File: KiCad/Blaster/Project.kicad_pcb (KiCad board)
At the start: 2 copper layers, 129.7 x 40.6 mm, 60 parts, among them J2 Power & Output Test Points, J3 Inputs Test Points, Q1 BUK9832-55A, Q2 BUK9832-55A, Q3 BUK9832-55A, SW1 Power, SW2 Fire, SW3 Freq Select, SW4 Fire Select, U1 TLV1117-50, U2 PIC16F1788-IP, U3 Audio Board

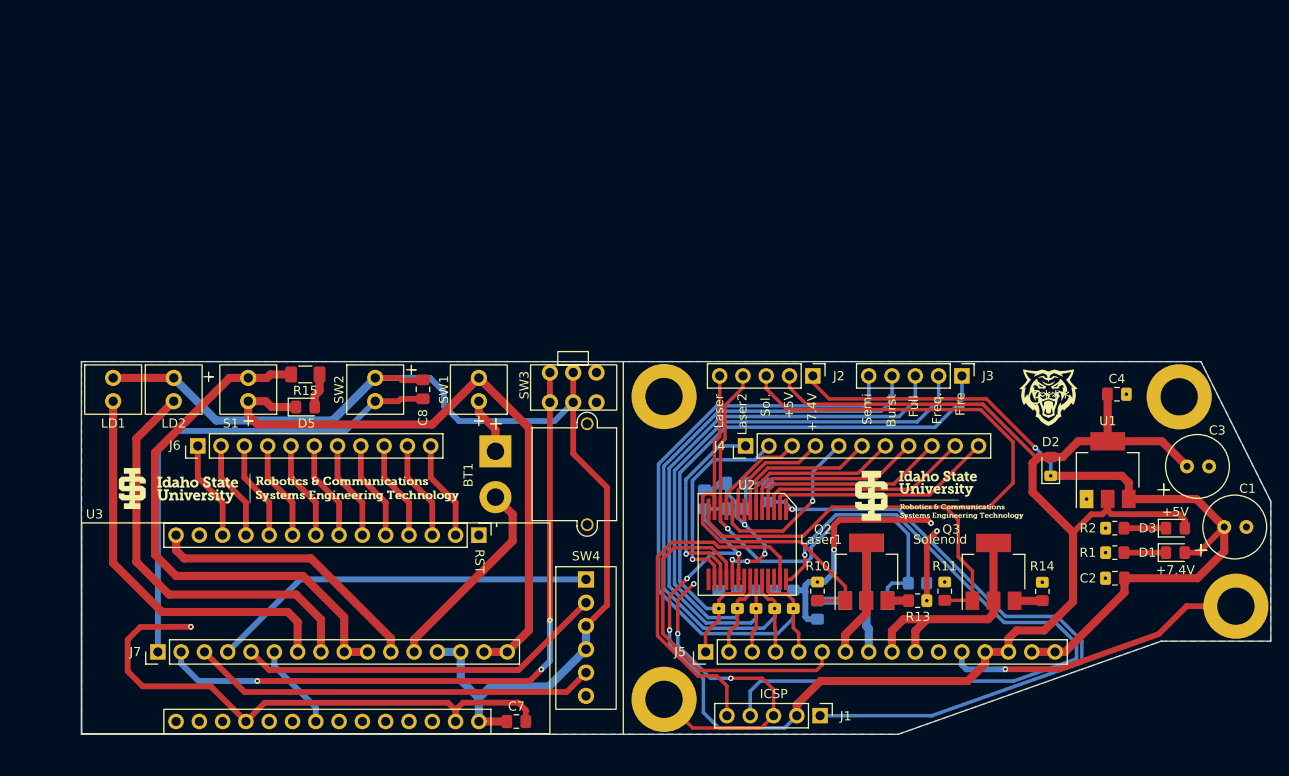
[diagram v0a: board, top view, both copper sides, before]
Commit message: Assign blaster footprints, Create Blaster PCB Outline
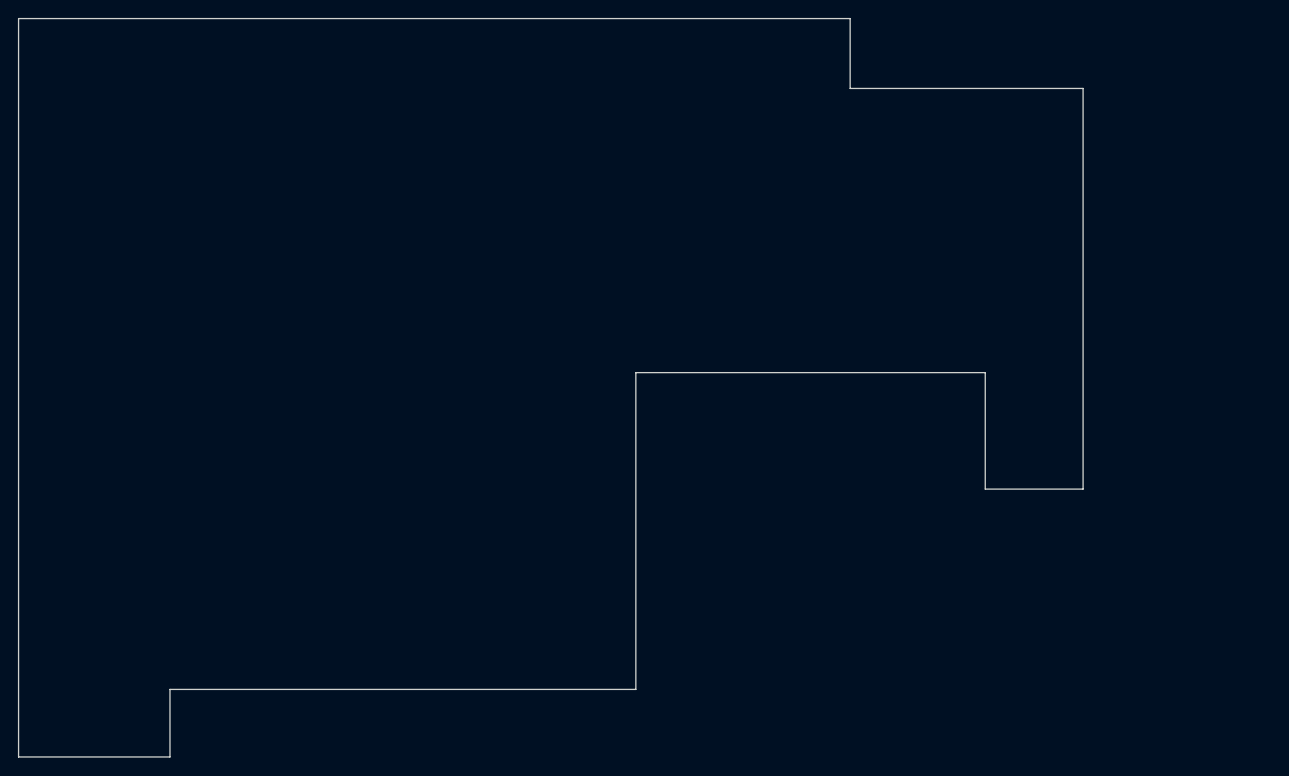
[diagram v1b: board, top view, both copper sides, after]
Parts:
- removed ? (x3): , 
- removed BT1: 7.4V, AlexWheelockFootprintLibrary:Project_Battery_Connector
- removed C1, C3: 220uF, AlexWheelockFootprintLibrary:Project_16V_220uF_Capacitor
- removed C2, C4: 0.1uF, Capacitor_SMD:C_0805_2012Metric_Pad1.18x1.45mm_HandSolder
- removed C5, C6, C7: 1uF, Capacitor_SMD:C_0805_2012Metric_Pad1.18x1.45mm_HandSolder
- removed C8: 50pF, Capacitor_SMD:C_0805_2012Metric_Pad1.18x1.45mm_HandSolder
- removed D1: +7.4V, LED_SMD:LED_0805_2012Metric_Pad1.15x1.40mm_HandSolder
- removed D2, D4, D5: 1N4148, Diode_SMD:D_0805_2012Metric_Pad1.15x1.40mm_HandSolder
- removed D3: +5V, LED_SMD:LED_0805_2012Metric_Pad1.15x1.40mm_HandSolder
- removed G*** (x7): LOGO, LOGO
- removed J1: ~, Connector_PinHeader_2.54mm:PinHeader_1x05_P2.54mm_Vertical
- removed J2: Power & Output Test Points, Connector_PinHeader_2.54mm:PinHeader_1x05_P2.54mm_Vertical
- removed J3: Inputs Test Points, Connector_PinHeader_2.54mm:PinHeader_1x05_P2.54mm_Vertical
- removed J4, J6: ~, Connector_PinHeader_2.54mm:PinHeader_1x11_P2.54mm_Vertical
- removed J5, J7: ~, Connector_PinHeader_2.54mm:PinHeader_1x16_P2.54mm_Vertical
- removed LD1, LD2: Laser Diode, AlexWheelockFootprintLibrary:Project_Locking_Output_Header
- removed Q1, Q2, Q3: BUK9832-55A, Package_TO_SOT_SMD:SOT-223-3_TabPin2
- removed R1: 8.2kΩ, Resistor_SMD:R_0805_2012Metric_Pad1.20x1.40mm_HandSolder
- removed R10, R11, R9: 100kΩ, Resistor_SMD:R_0805_2012Metric_Pad1.20x1.40mm_HandSolder
- removed R12, R13, R14: 0Ω, Resistor_SMD:R_0805_2012Metric_Pad1.20x1.40mm_HandSolder
- removed R15: 1kΩ, Resistor_SMD:R_1206_3216Metric_Pad1.30x1.75mm_HandSolder
- removed R2: 4.7kΩ, Resistor_SMD:R_0805_2012Metric_Pad1.20x1.40mm_HandSolder
- removed R3: 10kΩ, Resistor_SMD:R_0805_2012Metric_Pad1.20x1.40mm_HandSolder
- removed R4, R5, R6, R7, R8: 330Ω, Resistor_SMD:R_0805_2012Metric_Pad1.20x1.40mm_HandSolder
- removed REF**: 6-32 Mount, AlexWheelockFootprintLibrary:6-32 Mount
- removed S1: Solenoid, AlexWheelockFootprintLibrary:Project_Locking_Output_Header
- removed SW1: Power, AlexWheelockFootprintLibrary:Project_Locking_Output_Header
- removed SW2: Fire, AlexWheelockFootprintLibrary:Project_Locking_Output_Header
- removed SW3: Freq Select, AlexWheelockFootprintLibrary:Project_Blaster_Freq_Switch
- removed SW4: Fire Select, AlexWheelockFootprintLibrary:Project_Locking_Header_1x06
- removed U1: TLV1117-50, Package_TO_SOT_SMD:SOT-223-3_TabPin2
- removed U2: PIC16F1788-IP, AlexWheelockFootprintLibrary:SSOP-28
- removed U3: Audio Board, AlexWheelockFootprintLibrary:Project_Audio_Board
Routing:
- net GND: track 239.0 -> 0.00 mm, vias 12 -> 0
- net +5V: track 176.0 -> 0.00 mm, vias 3 -> 0
- net +5V_Top: track 123.6 -> 0.00 mm
- net +7.4V: track 88.6 -> 0.00 mm, vias 1 -> 0
- net Net-(Q3-G): track 87.3 -> 0.00 mm
- net RB7: track 82.4 -> 0.00 mm, vias 1 -> 0
- net Frequency Select_Top: track 74.7 -> 0.00 mm, vias 3 -> 0
- net Net-(D4-K): track 73.1 -> 0.00 mm, vias 1 -> 0
- net Semi-Auto: track 71.0 -> 0.00 mm
- net +7.4V_Top: track 70.3 -> 0.00 mm
- net Burst: track 67.9 -> 0.00 mm
- net Full-Auto: track 65.9 -> 0.00 mm
- net Frequency Select: track 65.4 -> 0.00 mm
- net Fire: track 64.8 -> 0.00 mm
- net Solenoid_Top: track 59.3 -> 0.00 mm
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- removed copper zone on B.Cu, net GND
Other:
- board size 129.7 x 40.6 mm -> 116.1 x 80.5 mm
- board text added: "TOP HATCH"
- board text removed: "+5V"
- board text removed: "+7.4V"
- board text removed: "Burst"
- board text removed: "Fire"
- board text removed: "Freq."
- board text removed: "Full"
- board text removed: "GitHub"
- board text removed: "ICSP"
- board text removed: "Laser"
- board text removed: "Laser Arcade Blaster (Bottom) Rev. A Alex Wheelock Spring 2025"
- board text removed: "Laser Arcade Blaster (Top) Rev. A Alex Wheelock Spring 2025"
- board text removed: "Laser1"
- board text removed: "Laser2"
- board text removed: "RST"
- board text removed: "Semi"
- board text removed: "Sol."
- board text removed: "Solenoid"

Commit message: Assign blaster PCB Footprints
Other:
- board text added: "Button Line"
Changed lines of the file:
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@@
+	)
+	(gr_line
+		(start 50.292 96.012)
+		(end 136.906 96.012)
+		(stroke
+			(width 0.1)
+			(type default)
+		)
+		(layer "B.Fab")
 	)
 	(gr_line
@@
 		(layer "F.Fab")
 	)
+	(gr_text "Button Line"
+		(at 58.928 96.012 0)
+		(layer "B.Fab")
+		(effects
+			(font
+				(size 1 1)
+				(thickness 0.15)
+			)
+			(justify left bottom mirror)
+		)
+	)
 	(gr_text "TOP HATCH"

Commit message: Place major components on PCB
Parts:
- added BT1: 18650, Battery:BatteryHolder_Keystone_1042_1x18650, F.Cu at (131.8, 61.7)
- added C1: 4.7µF, Capacitor_SMD:C_0805_2012Metric_Pad1.18x1.45mm_HandSolder, F.Cu at (-32.5, 95.3)
- added C10: 1uF, Capacitor_SMD:C_0805_2012Metric_Pad1.18x1.45mm_HandSolder, F.Cu at (-29.1, 167.0)
- added C11: 1uF, Capacitor_SMD:C_0805_2012Metric_Pad1.18x1.45mm_HandSolder, F.Cu at (-29.1, 170.0)
- added C12: 10nF, Capacitor_SMD:C_0805_2012Metric_Pad1.18x1.45mm_HandSolder, F.Cu at (-20.5, 123.6)
- added C13: 4.7µF, Capacitor_SMD:C_0805_2012Metric_Pad1.18x1.45mm_HandSolder, F.Cu at (-20.5, 126.6)
- added C14: 0.1µF, Capacitor_SMD:C_0805_2012Metric_Pad1.18x1.45mm_HandSolder, F.Cu at (-20.5, 129.6)
- added C15: 0.1µF, Capacitor_SMD:C_0805_2012Metric_Pad1.18x1.45mm_HandSolder, F.Cu at (-20.5, 132.6)
- added C16: 47pF, Capacitor_SMD:C_0805_2012Metric_Pad1.18x1.45mm_HandSolder, F.Cu at (-20.5, 135.6)
- added C17: 47pF, Capacitor_SMD:C_0805_2012Metric_Pad1.18x1.45mm_HandSolder, F.Cu at (-20.5, 138.6)
- added C2: 4.7µF, Capacitor_SMD:C_0805_2012Metric_Pad1.18x1.45mm_HandSolder, F.Cu at (-32.5, 98.3)
- added C3: 0.1µF, Capacitor_SMD:C_0805_2012Metric_Pad1.18x1.45mm_HandSolder, F.Cu at (-32.5, 101.3)
- added C4: 4.7µF, Capacitor_SMD:C_0805_2012Metric_Pad1.18x1.45mm_HandSolder, F.Cu at (-32.5, 104.3)
- added C5: 4.7µF, Capacitor_SMD:C_0805_2012Metric_Pad1.18x1.45mm_HandSolder, F.Cu at (-32.5, 107.3)
- added C6: 0.1µF, Capacitor_SMD:C_0805_2012Metric_Pad1.18x1.45mm_HandSolder, F.Cu at (-32.5, 110.3)
- added C7: 22µF, Capacitor_SMD:C_0805_2012Metric_Pad1.18x1.45mm_HandSolder, F.Cu at (-32.5, 113.3)
- added C8: 0.1µF, Capacitor_SMD:C_0805_2012Metric_Pad1.18x1.45mm_HandSolder, F.Cu at (-32.5, 116.3)
- added C9: 470pF, Capacitor_SMD:C_0805_2012Metric_Pad1.18x1.45mm_HandSolder, F.Cu at (113.8, 79.1)
- added D1: Charge, LED_SMD:LED_0805_2012Metric_Pad1.15x1.40mm_HandSolder, F.Cu at (10.3, 113.9)
- added D2: 1N4148, Diode_SMD:D_0805_2012Metric_Pad1.15x1.40mm_HandSolder, F.Cu at (-29.1, 173.0)
- added D3: IN-P32TRRRGB, 0_AKeller_Footprints:IN-P32TRRRGB, B.Cu at (117.9, 89.7)
- added D4: IN-P32TRRRGB, 0_AKeller_Footprints:IN-P32TRRRGB, B.Cu at (83.9, 85.8)
- added D5: TX, LED_SMD:LED_0805_2012Metric_Pad1.15x1.40mm_HandSolder, F.Cu at (-20.5, 141.6)
- added D6: RX, LED_SMD:LED_0805_2012Metric_Pad1.15x1.40mm_HandSolder, F.Cu at (-20.5, 144.7)
- added J1: +12V, 0_AKeller_Footprints:AMASS_XT60PW-M_1x02_P7.20mm_Horizontal, F.Cu at (77.1, 110.5)
- added J2: Speaker, 0_AKeller_Footprints:1x2_100mil_Header_Locking, F.Cu at (68.5, 83.7)
- added J3: ICSP, 0_AKeller_Footprints:1x6_100mil_Header, F.Cu at (-65.9, 172.4)
- added J4: Solenoid, 0_AKeller_Footprints:1x2_100mil_Header_Locking, F.Cu at (178.2, 51.6)
- added J5: Laser, 0_AKeller_Footprints:1x2_100mil_Header_Locking, F.Cu at (68.5, 46.4)
- added J6: Laser, 0_AKeller_Footprints:1x2_100mil_Header_Locking, F.Cu at (68.5, 56.9)
- added J7: USB_B_Micro, 0_AKeller_Footprints:USB_Micro-B_Amphenol, F.Cu at (97.4, 41.2)
- added L1: 6.8µH, 0_AKeller_Footprints:LA Blaster Power Inductor, F.Cu at (-13.2, 108.5)
- added L2: 2.2µH, Inductor_SMD:L_0805_2012Metric_Pad1.15x1.40mm_HandSolder, F.Cu at (-12.1, 135.2)
- added Q1: DMG3402L, Package_TO_SOT_SMD:SOT-23, F.Cu at (68.5, 88.7)
- added Q2: DMG3402L, Package_TO_SOT_SMD:SOT-23, F.Cu at (72.2, 88.7)
- added Q3: DMG3402L, Package_TO_SOT_SMD:SOT-23, F.Cu at (178.2, 56.7)
- added Q4: DMG3402L, Package_TO_SOT_SMD:SOT-23, F.Cu at (-38.4, 137.6)
- added R1: 2.2kΩ, Resistor_SMD:R_0805_2012Metric_Pad1.20x1.40mm_HandSolder, F.Cu at (-10.2, 95.2)
- added R10: 10kΩ, Resistor_SMD:R_0805_2012Metric_Pad1.20x1.40mm_HandSolder, F.Cu at (-36.8, 149.2)
- added R11: 10kΩ, Resistor_SMD:R_0805_2012Metric_Pad1.20x1.40mm_HandSolder, F.Cu at (177.2, 60.8)
- added R12: 330Ω, Resistor_SMD:R_0805_2012Metric_Pad1.20x1.40mm_HandSolder, F.Cu at (178.1, 73.5)
- added R13: 330Ω, Resistor_SMD:R_0805_2012Metric_Pad1.20x1.40mm_HandSolder, F.Cu at (-36.8, 158.0)
- added R14: 330Ω, Resistor_SMD:R_0805_2012Metric_Pad1.20x1.40mm_HandSolder, F.Cu at (-36.8, 161.0)
- added R15: 330Ω, Resistor_SMD:R_0805_2012Metric_Pad1.20x1.40mm_HandSolder, F.Cu at (-32.0, 149.2)
- added R16: 20Ω, Resistor_SMD:R_0805_2012Metric_Pad1.20x1.40mm_HandSolder, F.Cu at (124.1, 89.0)
- added R17: 20Ω, Resistor_SMD:R_0805_2012Metric_Pad1.20x1.40mm_HandSolder, F.Cu at (114.2, 87.0)
- added R18: 0Ω, Resistor_SMD:R_0805_2012Metric_Pad1.20x1.40mm_HandSolder, F.Cu at (69.5, 41.1)
- added R19: 0Ω, Resistor_SMD:R_0805_2012Metric_Pad1.20x1.40mm_HandSolder, F.Cu at (69.5, 51.8)
- added R2: 2.2kΩ, Resistor_SMD:R_0805_2012Metric_Pad1.20x1.40mm_HandSolder, F.Cu at (-10.2, 98.2)
- added R20: 260Ω, Resistor_SMD:R_0805_2012Metric_Pad1.20x1.40mm_HandSolder, F.Cu at (111.9, 90.5)
- added R21: 20Ω, Resistor_SMD:R_0805_2012Metric_Pad1.20x1.40mm_HandSolder, F.Cu at (77.7, 86.5)
- added R22: 20Ω, Resistor_SMD:R_0805_2012Metric_Pad1.20x1.40mm_HandSolder, F.Cu at (80.2, 83.0)
- added R23: 10kΩ, Resistor_SMD:R_0805_2012Metric_Pad1.20x1.40mm_HandSolder, F.Cu at (-27.3, 158.0)
- added R24: 260Ω, Resistor_SMD:R_0805_2012Metric_Pad1.20x1.40mm_HandSolder, F.Cu at (87.7, 82.4)
- added R25: 3.3kΩ, Resistor_SMD:R_0805_2012Metric_Pad1.20x1.40mm_HandSolder, F.Cu at (-12.1, 138.1)
- added R26: 3.3kΩ, Resistor_SMD:R_0805_2012Metric_Pad1.20x1.40mm_HandSolder, F.Cu at (-12.1, 141.1)
- added R27: 10kΩ, Resistor_SMD:R_0805_2012Metric_Pad1.20x1.40mm_HandSolder, F.Cu at (-12.1, 144.0)
- added R3: 47kΩ, Resistor_SMD:R_0805_2012Metric_Pad1.20x1.40mm_HandSolder, F.Cu at (-10.2, 101.2)
- added R4: 15kΩ, Resistor_SMD:R_0805_2012Metric_Pad1.20x1.40mm_HandSolder, F.Cu at (-10.2, 104.1)
- added R5: 10kΩ, Resistor_SMD:R_0805_2012Metric_Pad1.20x1.40mm_HandSolder, F.Cu at (113.8, 75.6)
- added R6: 1kΩ, Resistor_SMD:R_0805_2012Metric_Pad1.20x1.40mm_HandSolder, F.Cu at (68.5, 93.8)
- added R7: 20kΩ, Resistor_SMD:R_0805_2012Metric_Pad1.20x1.40mm_HandSolder, F.Cu at (122.2, 86.1)
- added R8: 10kΩ, Resistor_SMD:R_0805_2012Metric_Pad1.20x1.40mm_HandSolder, F.Cu at (74.1, 84.3)
- added R9: 20kΩ, Resistor_SMD:R_0805_2012Metric_Pad1.20x1.40mm_HandSolder, F.Cu at (125.5, 86.1)
- added SW1: Charge, 0_AKeller_Footprints:T80-T, F.Cu at (143.5, 44.2)
- added SW2: Power, 0_AKeller_Footprints:LA Blaster Power Switch, B.Cu at (83.9, 96.0)
- added SW3: Trigger, Button_Switch_THT:SW_Tactile_SPST_Angled_PTS645Vx31-2LFS, F.Cu at (177.0, 82.2)
- added SW4: Single, Button_Switch_THT:SW_PUSH_6mm_H5mm, B.Cu at (124.4, 98.3)
- added SW5: Burst, Button_Switch_THT:SW_PUSH_6mm_H5mm, B.Cu at (105.1, 98.3)
- added SW6: Auto, Button_Switch_THT:SW_PUSH_6mm_H5mm, B.Cu at (114.7, 98.3)
- added TP1: +12V, 0_AKeller_Footprints:1x1_100mil_Header, F.Cu at (-5.98, 95.6)
- added TP10: MCLR, 0_AKeller_Footprints:1x1_100mil_Header, F.Cu at (-73.5, 165.1)
- added TP11: TRIG0, 0_AKeller_Footprints:1x1_100mil_Header, F.Cu at (104.4, 106.3)
- added TP12: TRIG1, 0_AKeller_Footprints:1x1_100mil_Header, F.Cu at (106.9, 106.3)
- added TP13: TRIG2, 0_AKeller_Footprints:1x1_100mil_Header, F.Cu at (109.5, 106.3)
- added TP14: TRIG3, 0_AKeller_Footprints:1x1_100mil_Header, F.Cu at (112.0, 106.3)
- added TP15: TRIG4, 0_AKeller_Footprints:1x1_100mil_Header, F.Cu at (114.6, 106.3)
- added TP16: Enable, 0_AKeller_Footprints:1x1_100mil_Header, F.Cu at (73.2, 79.3)
- added TP17: TRIG5, 0_AKeller_Footprints:1x1_100mil_Header, F.Cu at (117.1, 106.3)
- added TP18: Line In, 0_AKeller_Footprints:1x1_100mil_Header, F.Cu at (120.9, 78.1)
- added TP19: Solenoid, 0_AKeller_Footprints:1x1_100mil_Header, F.Cu at (-66.2, 161.5)
- added TP2: +5V, 0_AKeller_Footprints:1x1_100mil_Header, F.Cu at (-5.98, 99.2)
- added TP20: Trigger, 0_AKeller_Footprints:1x1_100mil_Header, F.Cu at (177.0, 77.4)
- added TP21: Activity, 0_AKeller_Footprints:1x1_100mil_Header, F.Cu at (124.7, 106.3)
- added TP22: Single, 0_AKeller_Footprints:1x1_100mil_Header, F.Cu at (-62.6, 154.2)
- added TP23: Burst, 0_AKeller_Footprints:1x1_100mil_Header, F.Cu at (-62.6, 157.8)
- added TP24: Auto, 0_AKeller_Footprints:1x1_100mil_Header, F.Cu at (-62.6, 161.5)
- added TP25: Auto LED, 0_AKeller_Footprints:1x1_100mil_Header, F.Cu at (-62.6, 165.1)
- added TP26: Burst LED, 0_AKeller_Footprints:1x1_100mil_Header, F.Cu at (-62.6, 168.7)
- added TP27: Single LED, 0_AKeller_Footprints:1x1_100mil_Header, F.Cu at (-59.0, 154.2)
- added TP28: Auto LED, 0_AKeller_Footprints:1x1_100mil_Header, F.Cu at (-59.0, 157.8)
- added TP29: Laser, 0_AKeller_Footprints:1x1_100mil_Header, F.Cu at (-59.0, 161.5)
- added TP3: Charge, 0_AKeller_Footprints:1x1_100mil_Header, F.Cu at (-2.34, 95.6)
- added TP30: Burst LED, 0_AKeller_Footprints:1x1_100mil_Header, F.Cu at (-59.0, 165.1)
- added TP31: Blue PWM, 0_AKeller_Footprints:1x1_100mil_Header, F.Cu at (-59.0, 168.7)
- added TP32: RX, 0_AKeller_Footprints:1x1_100mil_Header, F.Cu at (-16.3, 123.9)
- added TP33: TX, 0_AKeller_Footprints:1x1_100mil_Header, F.Cu at (-16.3, 127.5)
- added TP34: D+, 0_AKeller_Footprints:1x1_100mil_Header, F.Cu at (-16.3, 131.2)
- added TP35: D-, 0_AKeller_Footprints:1x1_100mil_Header, F.Cu at (-16.3, 134.8)
- added TP4: V_{BAT}, 0_AKeller_Footprints:1x1_100mil_Header, F.Cu at (-2.34, 99.2)
- added TP5: Power, 0_AKeller_Footprints:1x1_100mil_Header, F.Cu at (1.30, 95.6)
- added TP6: +3.3V, 0_AKeller_Footprints:1x1_100mil_Header, F.Cu at (1.30, 99.2)
- added TP7: 100kHz, 0_AKeller_Footprints:1x1_100mil_Header, F.Cu at (109.9, 75.6)
- added TP8: Ramp, 0_AKeller_Footprints:1x1_100mil_Header, F.Cu at (120.9, 75.6)
- added TP9: Audio PWM, 0_AKeller_Footprints:1x1_100mil_Header, F.Cu at (106.0, 75.6)
- added U1: TLV1117-50, Package_TO_SOT_SMD:SOT-223-3_TabPin2, F.Cu at (106.3, 24.4)
- added U2: MCP73831-2-OT, Package_TO_SOT_SMD:SOT-23-5_HandSoldering, F.Cu at (4.95, 114.9)
- added U3: LMR51635, Package_TO_SOT_SMD:SOT-23-6_Handsoldering, F.Cu at (4.97, 110.1)
- added U4: MCP6002, Package_SO:SOIC-8_3.9x4.9mm_P1.27mm, F.Cu at (127.8, 77.5)
- added U5: Audio FX Mini, 0_AKeller_Footprints:Adafruit_AudioFXMini, F.Cu at (114.6, 93.0)
- added U6: PIC16LF1788, 0_AKeller_Footprints:SSOP-28, F.Cu at (-21.8, 73.0)
- added U7: FT232RL, 0_AKeller_Footprints:SSOP-28, F.Cu at (-8.17, 127.9)

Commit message: Complete Blaster PCB layout and traces
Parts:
- removed the TP10 at (-73.5, 165.1)
- removed the TP22 at (-62.6, 154.2)
- removed the TP23 at (-62.6, 157.8)
- removed TP24: Auto, 0_AKeller_Footprints:1x1_100mil_Header
- removed TP25, TP28: Auto LED, 0_AKeller_Footprints:1x1_100mil_Header
- removed TP26, TP30: Burst LED, 0_AKeller_Footprints:1x1_100mil_Header
- removed TP27: Single LED, 0_AKeller_Footprints:1x1_100mil_Header
- removed TP31: Blue PWM, 0_AKeller_Footprints:1x1_100mil_Header
- removed TP34: D+, 0_AKeller_Footprints:1x1_100mil_Header
- removed TP35: D-, 0_AKeller_Footprints:1x1_100mil_Header
- removed the TP8 at (120.9, 75.6)
- removed the TP9 at (106.0, 75.6)
- added D2: Tether, LED_SMD:LED_0805_2012Metric_Pad1.15x1.40mm_HandSolder, F.Cu at (117.3, 40.0)
- added D3: Power, LED_SMD:LED_0805_2012Metric_Pad1.15x1.40mm_HandSolder, F.Cu at (106.4, 40.9)
- added G***: LOGO, 2025 Logos:RCET Horizontal 0-15x1-01, F.Cu at (110.0, 109.6)
- added G***: LOGO, 2025 Logos:Benny_0-23x0-24, F.Cu at (77.5, 48.4)
- added G***: LOGO, 2025 Logos:AKeller_Logo_0-4x0-3, F.Cu at (149.6, 51.1)
- added G***: LOGO, 2025 Logos:LA_QR_Code_0-5x0-5, F.Cu at (146.4, 65.5)
- added G***: LOGO, 2025 Logos:AKeller_Logo_0-4x0-3, B.Cu at (78.0, 44.1)
- added G***: LOGO, 2025 Logos:RCET Stacked 0-25x0_76, B.Cu at (156.0, 50.9)
- added G***: LOGO, 2025 Logos:LA_QR_Code_0-5x0-5, B.Cu at (146.2, 65.9)
- added G***: LOGO, 2025 Logos:Benny_0-23x0-24, B.Cu at (74.2, 67.4)
- added R2: 1kΩ, Resistor_SMD:R_0805_2012Metric_Pad1.20x1.40mm_HandSolder, B.Cu at (117.3, 42.0)
- added R5: 1kΩ, Resistor_SMD:R_0805_2012Metric_Pad1.20x1.40mm_HandSolder, B.Cu at (106.4, 44.1)
- added REF**: M3 Mounting, 0_AKeller_Footprints:M3 Mounting, F.Cu at (69.1, 51.9)
- added REF**: M3 Mounting, 0_AKeller_Footprints:M3 Mounting, F.Cu at (69.1, 102.7)
- added REF**: M3 Mounting, 0_AKeller_Footprints:M3 Mounting, F.Cu at (140.7, 51.9)
- added TP18: Red, 0_AKeller_Footprints:1x1_100mil_Header, F.Cu at (81.0, 67.2)
- added TP21: Blue, 0_AKeller_Footprints:1x1_100mil_Header, F.Cu at (81.0, 64.0)
- C10, C11, C12, C13, C14, C15, C16, C17, C4, Q1, Q2, Q3, R1, U6, U7: moved to B.Cu
- D4: renamed from D2; moved to B.Cu
- R10: renamed from R8; moved to B.Cu
- R12: renamed from R10; moved to B.Cu
- R13: renamed from R11; moved to B.Cu
- R14: renamed from R12; moved to B.Cu
- R21: renamed from R19; moved to B.Cu
- R22: renamed from R20; moved to B.Cu
- R27: renamed from R25; moved to B.Cu
- R28: renamed from R26; moved to B.Cu
- R3: renamed from R2; moved to B.Cu
- R8: renamed from R6; moved to B.Cu
- SW1: value Charge -> Charge Source
- TP20: value Trigger -> Green
- moved TP16 265.2 mm to (178.4, 59.1)
- moved J3 264.1 mm to (178.2, 71.4), turned to -90 degrees
- moved C2 205.3 mm to (167.8, 49.9)
- moved C10 187.5 mm to (129.2, 66.5), turned to 180 degrees
- moved D4 184.1 mm to (125.1, 72.5)
- moved C11 182.3 mm to (127.1, 76.1)
- moved R12 181.9 mm to (127.1, 70.2), turned to 180 degrees
- moved R15 172.8 mm to (126.7, 102.1), turned to -90 degrees
- moved C1 172.5 mm to (133.9, 52.6), turned to -90 degrees
- moved R16 165.5 mm to (117.9, 102.0), turned to -90 degrees
- moved TP3 164.1 mm to (148.6, 44.2)
- moved C4 159.6 mm to (119.0, 54.0)
- moved TP19 153.1 mm to (67.7, 75.3)
- moved D8 151.9 mm to (90.4, 40.9)
- moved C14 149.6 mm to (108.6, 54.1), turned to 90 degrees
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- renumbered C2 to C1, C1 to C2, D3 to D5, D4 to D6, D5 to D7, D6 to D8, R9 to R11, R13 to R15, R14 to R16, R15 to R17, R16 to R18, R17 to R19, R18 to R20, R21 to R23, R22 to R24, R23 to R25, R24 to R26, R27 to R29, R3 to R4, R4 to R6, R5 to R7, R7 to R9, TP3 to TP1, TP13 to TP10, TP14 to TP11, TP15 to TP12, TP16 to TP13, TP17 to TP14, TP18 to TP15, TP19 to TP16, TP21 to TP17, TP29 to TP19, TP1 to TP2, TP32 to TP22, TP33 to TP23, TP2 to TP3, TP11 to TP8, TP12 to TP9
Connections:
- C2 pad 1: Net-(SW1-A) -> Net-(SW1-C)
- J3 pad 2: +5V -> +3V3
- R12 pad 1: +5V -> +3V3
- SW1 pad 1: Net-(SW1-A) -> VBUS
- SW1 pad 3: VBUS -> Net-(SW1-C)
- TP20 pad 1: Net-(U6-P1C/AN10/RB1) -> Green PWM
- TP3 pad 1: Net-(SW1-A) -> Net-(SW1-C)
- U1 pad 2: Net-(SW1-A) -> Net-(SW1-C)
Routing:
- net +3V3: track 0.00 -> 413.1 mm, vias 0 -> 1
- net +12V: track 0.00 -> 241.0 mm
- net GND: track 0.00 -> 218.6 mm, vias 0 -> 2
- net TX: track 0.00 -> 129.8 mm, vias 0 -> 2
- net RX: track 0.00 -> 110.8 mm
- net Net-(U6-P1B/AN8/RB2): track 0.00 -> 94.8 mm
- net Net-(U6-PGM/C12IN2-/AN8/RB3): track 0.00 -> 94.6 mm
- net 100kHz: track 0.00 -> 94.6 mm, vias 0 -> 1
- net VBUS: track 0.00 -> 87.1 mm
- net Net-(U6-P1D/AN11/RB4): track 0.00 -> 82.2 mm
- net Net-(BT1-+): track 0.00 -> 77.6 mm
- net Net-(Q3-G): track 0.00 -> 77.0 mm, vias 0 -> 1
- net Net-(U6-P1C/AN10/RB1): track 0.00 -> 74.7 mm
- net Net-(D4-K): track 0.00 -> 67.5 mm, vias 0 -> 1
- net Green PWM: track 0.00 -> 61.3 mm, vias 0 -> 1
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- added copper zone on B.Cu, net GND
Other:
- board text added: "+"
- board text added: "Laser Arcade Blaster Rev. B - Fall 2025 Andrew Keller"
- board text added: "MODE"
- board text added: "Player"
